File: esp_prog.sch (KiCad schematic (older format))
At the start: 7 parts, among them J1 10118192-0002LF, J2 Conn_01x06_Female, U1 CP2102N-A01-GQFN28, U2 SPX3819M5-L

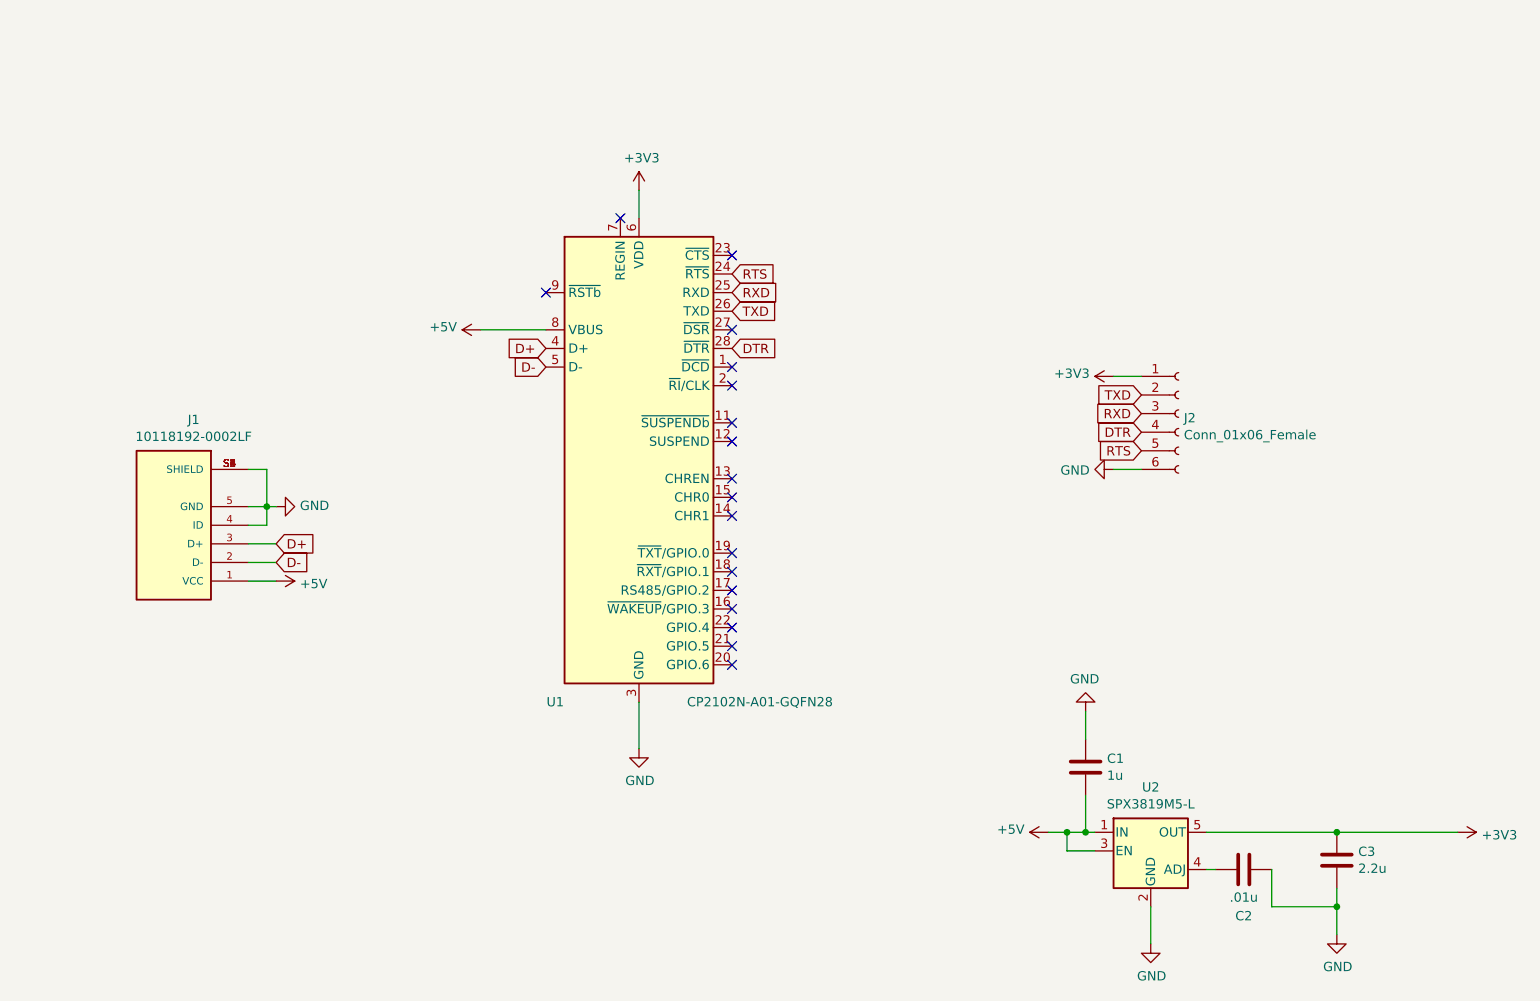
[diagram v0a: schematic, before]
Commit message: v2, need to add leds and things
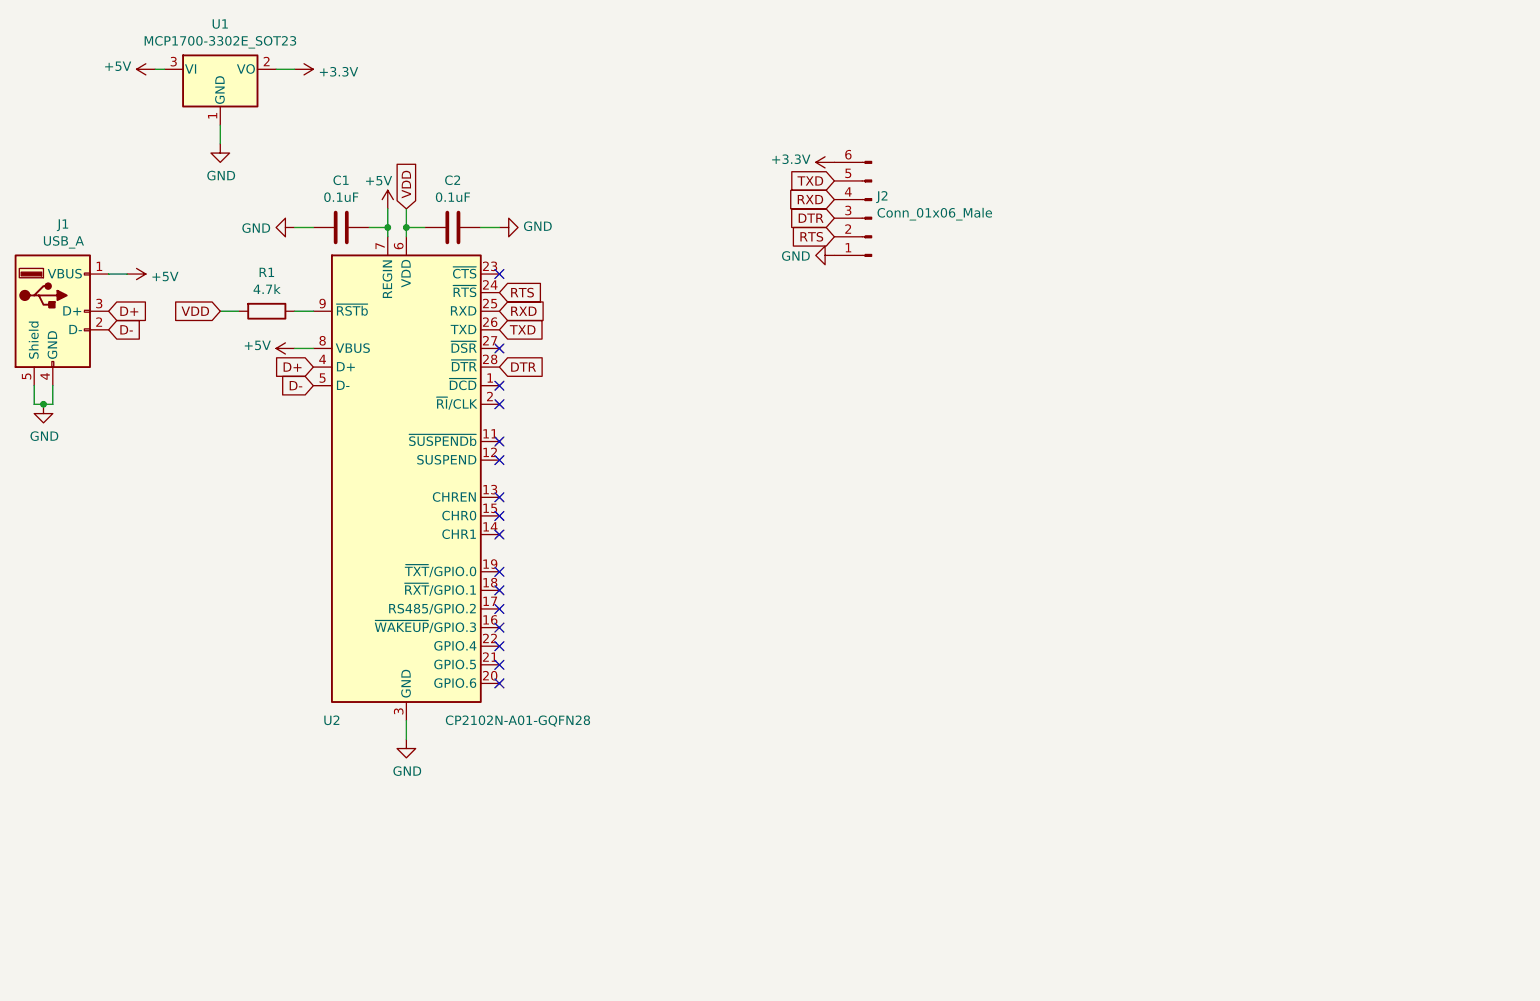
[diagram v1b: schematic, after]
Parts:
- removed C3: 2.2u, Capacitor_SMD:C_0603_1608Metric_Pad1.08x0.95mm_HandSolder, symbol Device:C
- removed J1: 10118192-0002LF, wled:AMPHENOL_10118192-0002LF, symbol 10118192-0002LF:10118192-0002LF
- removed J2: Conn_01x06_Female, Connector_JST:JST_XH_B6B-XH-A_1x06_P2.50mm_Vertical, symbol Connector:Conn_01x06_Female
- removed U1: CP2102N-A01-GQFN28, Package_DFN_QFN:QFN-28-1EP_5x5mm_P0.5mm_EP3.35x3.35mm, symbol Interface_USB:CP2102N-A01-GQFN28
- removed U2: SPX3819M5-L, Package_TO_SOT_SMD:SOT-23-5, symbol Regulator_Linear:SPX3819M5-L
- added J1: USB_A, Connector_USB:USB_A_CNCTech_1001-011-01101_Horizontal, symbol Connector:USB_A
- added J2: Conn_01x06_Male, Connector_JST:JST_XH_B6B-XH-A_1x06_P2.50mm_Vertical, symbol Connector:Conn_01x06_Male
- added R1: 4.7k, Resistor_SMD:R_0603_1608Metric_Pad0.98x0.95mm_HandSolder, symbol Device:R
- added U1: MCP1700-3302E_SOT23, Package_TO_SOT_SMD:SOT-23, symbol Regulator_Linear:MCP1700-3302E_SOT23
- added U2: CP2102N-A01-GQFN28, Package_DFN_QFN:QFN-28-1EP_5x5mm_P0.5mm_EP3.35x3.35mm, symbol Interface_USB:CP2102N-A01-GQFN28
- C1: value 1u -> 0.1uF
- C2: value .01u -> 0.1uF
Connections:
- net +3V3: now also J2.6 (Pin_6), U1.2 (VO)
- net +5V: now also J1.1 (VBUS), U1.3 (VI), U2.7 (REGIN), U2.8 (VBUS)
- net D+: now also J1.3 (D+), U2.4 (D+)
- net D-: now also J1.2 (D-), U2.5 (D-)
- net DTR: now also J2.3 (Pin_3), U2.28 (~DTR)
- net GND: now also C2.2, J1.4 (GND), J1.5 (Shield), J2.1 (Pin_1), U1.1 (GND), U2.29 (GND), U2.3 (GND); no longer C2.1
- net RTS: now also J2.2 (Pin_2), U2.24 (~RTS)
- net RXD: now also J2.4 (Pin_4), U2.25 (RXD)
- net TXD: now also J2.5 (Pin_5), U2.26 (TXD)
- new net: R1.1, U2.9 (~RSTb)
- new net VDD: C2.1, R1.2, U2.6 (VDD)
- no-connect marks 18 -> 16
